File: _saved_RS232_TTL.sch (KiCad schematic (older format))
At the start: 11 parts, among them J1 TB_1X2, J2 TB_1X2, J3 TB_1X2, J4 TB_1X2, P1 CONN_02X02, U1 ST3232E

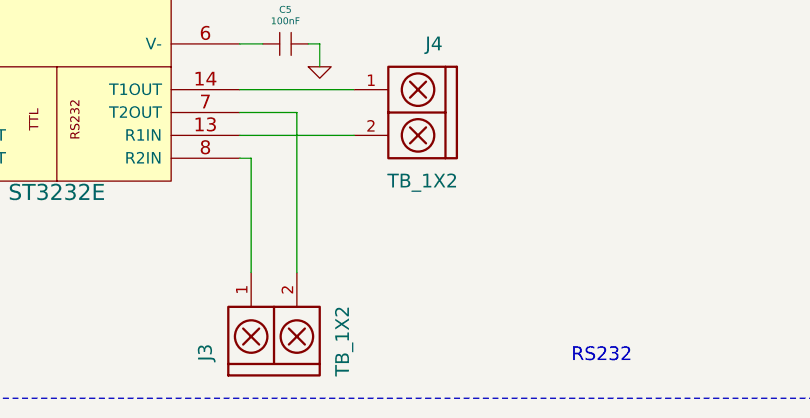
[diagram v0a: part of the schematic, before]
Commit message: Ruteo del PCB, agrego una salida de 5v y 3v en el esquematico
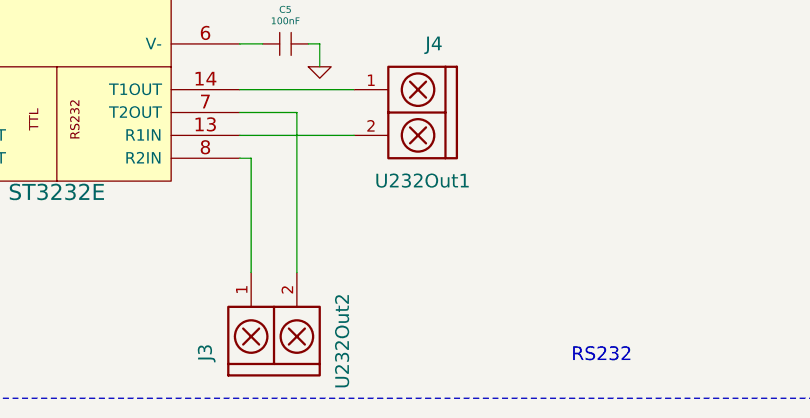
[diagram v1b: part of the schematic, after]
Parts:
- J3: value TB_1X2 -> U232Out2
- J4: value TB_1X2 -> U232Out1
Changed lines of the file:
@@
 P 6450 4050
 F 0 "J4" H 6450 4350 60  0000 C CNN
-F 1 "TB_1X2" H 6500 3750 60  0000 C CNN
+F 1 "U232Out1" H 6500 3750 60  0000 C CNN
 F 2 "Connect:AK300-2" H 6400 4100 60  0001 C CNN
 F 3 "" H 6400 4100 60  0000 C CNN
@@
 P 5750 5100
 F 0 "J3" H 5750 5400 60  0000 C CNN
-F 1 "TB_1X2" H 5800 4800 60  0000 C CNN
+F 1 "U232Out2" H 5800 4800 60  0000 C CNN
 F 2 "Connect:AK300-2" H 5700 5150 60  0001 C CNN
 F 3 "" H 5700 5150 60  0000 C CNN
